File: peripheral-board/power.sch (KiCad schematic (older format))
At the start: 37 parts, among them CON4001 BARREL_JACK, Q4001 IRLML2244TRPbF, U4001 AP1509, U4002 LM27313, U4003 LT3652

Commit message: minor fixes
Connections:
- no-connect marks 0 -> 1
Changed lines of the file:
@@
-$EndComp
-$Comp
-L PWR_FLAG #FLG061
-U 1 1 58A910EB
-P 1850 1750
-F 0 "#FLG061" H -900 525 50  0001 C CNN
-F 1 "PWR_FLAG" H 1850 1924 50  0000 C CNN
-F 2 "" H -900 450 50  0001 C CNN
-F 3 "" H -900 450 50  0001 C CNN
-	1    1850 1750
-	0    1    1    0
 $EndComp
 $Comp
@@
 Text Label 6000 2400 0    60   ~ 0
 CHRG_SENSE
+Connection ~ 10350 1650
+NoConn ~ 1800 1650
+$Comp
+L PWR_FLAG #FLG061
+U 1 1 58A9FA40
+P 5350 1000
+F 0 "#FLG061" H -1000 225 50  0001 C CNN
+F 1 "PWR_FLAG" H 5350 1174 50  0000 C CNN
+F 2 "" H -1000 150 50  0001 C CNN
+F 3 "" H -1000 150 50  0001 C CNN
+	1    5350 1000
+	1    0    0    -1
+$EndComp
+$Comp
+L PWR_FLAG #FLG062
+U 1 1 58A9FB2F
+P 5250 1550
+F 0 "#FLG062" H -1100 775 50  0001 C CNN
+F 1 "PWR_FLAG" H 5250 1724 50  0000 C CNN
+F 2 "" H -1100 700 50  0001 C CNN
+F 3 "" H -1100 700 50  0001 C CNN
+	1    5250 1550
+	1    0    0    -1
+$EndComp
 $EndSCHEMATC

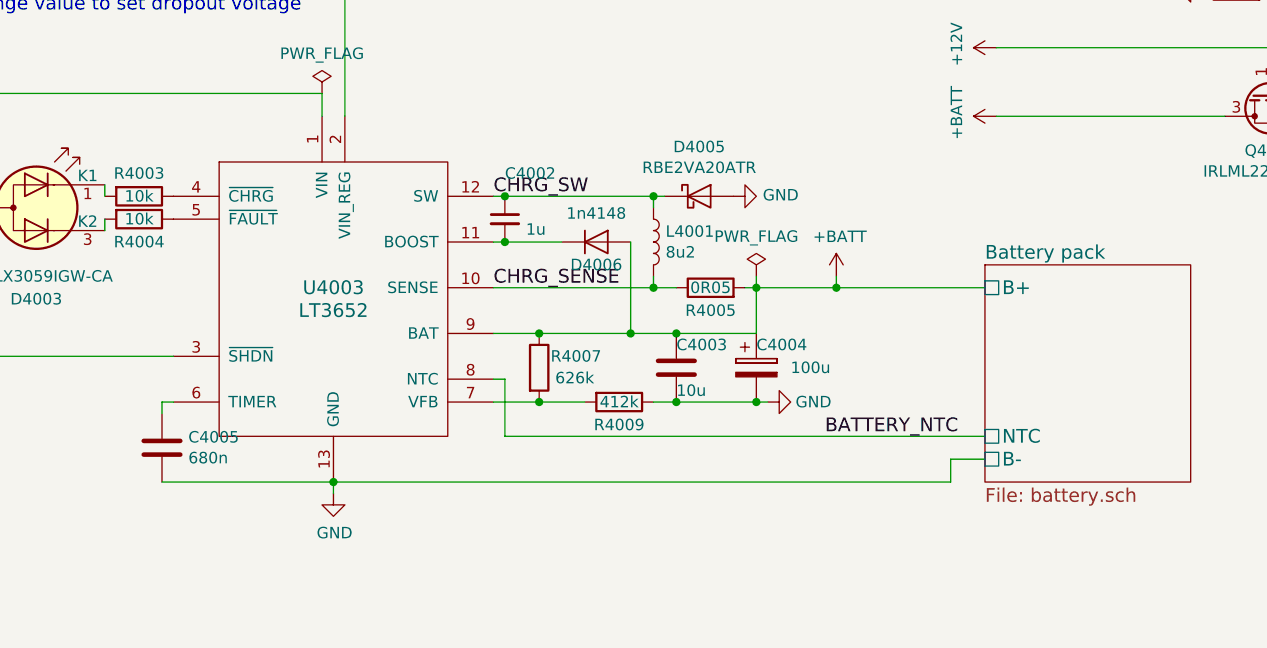
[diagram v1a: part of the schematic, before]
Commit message: added speaker and battery connectors
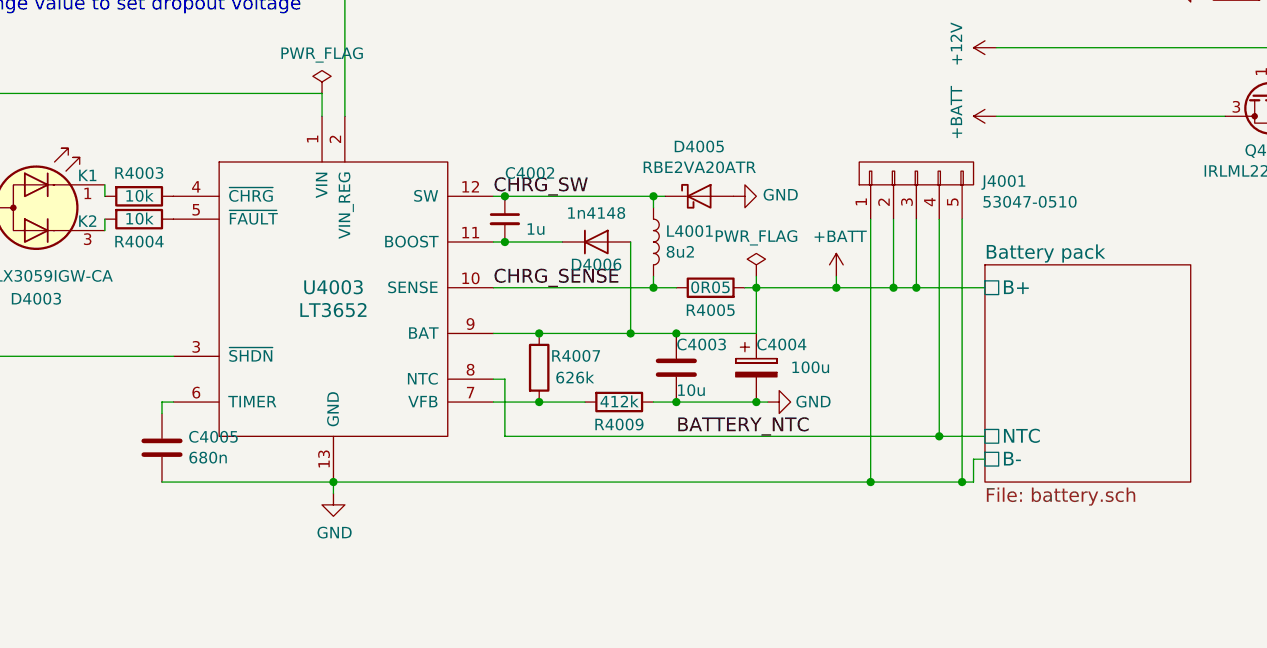
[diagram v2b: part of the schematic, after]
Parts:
- added J4001: 53047-0510, Connectors_Molex:Connector_Molex_PicoBlade_53047-0510, symbol CONN_01X05
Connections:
- net +BATT: now also J4001.2 (P2), J4001.3 (P3)
- net BATTERY_NTC: now also J4001.4 (P4)
- net GND: now also J4001.1 (P1), J4001.5 (P5)
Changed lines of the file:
@@
 Text Notes 2000 2750 0    60   ~ 0
 Add shutdown input\n
-Text Label 7450 3050 0    60   ~ 0
+Text Label 6800 3050 0    60   ~ 0
 BATTERY_NTC
 $Comp
@@
 	1    0    0    -1
 $EndComp
-Wire Wire Line
-	6700 2900 7200 2900
-Connection ~ 7150 2900
-Connection ~ 6800 2900
-Wire Wire Line
-	7150 2600 6000 2600
-Connection ~ 6800 2600
-Connection ~ 6200 2600
-Wire Wire Line
-	6000 2900 6400 2900
-Connection ~ 6200 2900
-Wire Wire Line
-	6000 2800 6050 2800
-Wire Wire Line
-	6000 2400 6800 2400
-Wire Wire Line
-	6700 2400 6700 2350
-Wire Wire Line
-	7150 2350 7150 2600
-Wire Wire Line
-	7100 2400 8150 2400
-Connection ~ 6700 2400
-Connection ~ 7150 2400
-Wire Wire Line
-	6700 2050 6700 2000
-Wire Wire Line
-	6000 2000 6750 2000
-Connection ~ 6700 2000
-Connection ~ 6050 2000
-Wire Wire Line
-	6000 2200 6300 2200
-Connection ~ 6050 2200
-Wire Wire Line
-	6600 2200 6600 2600
-Connection ~ 6600 2600
-Wire Wire Line
-	7500 2350 7500 2400
-Connection ~ 7500 2400
-Wire Wire Line
-	4600 2900 4550 2900
-Wire Wire Line
-	4550 2900 4550 2950
-Wire Wire Line
-	5250 1650 5250 1550
-Wire Wire Line
-	5250 1550 3700 1550
-Wire Wire Line
-	1800 1550 3400 1550
-Wire Wire Line
-	3300 1350 3300 1600
-Connection ~ 3300 1550
-Wire Wire Line
-	4600 2700 3050 2700
-Wire Wire Line
-	3050 2650 3050 2750
-Connection ~ 3050 2700
-Wire Wire Line
-	3050 1000 3050 2350
-Wire Wire Line
-	3050 1000 5350 1000
-Wire Wire Line
-	5350 1000 5350 1650
-Wire Wire Line
-	3300 1050 3300 1000
-Connection ~ 3300 1000
-Wire Wire Line
-	1800 1750 1850 1750
-Wire Wire Line
-	1850 1750 1850 1800
-Wire Wire Line
-	1850 1550 1850 1300
-Wire Wire Line
-	2150 1550 2150 1300
-Connection ~ 1850 1550
-Connection ~ 2150 1550
-Wire Wire Line
-	8150 3050 6050 3050
-Wire Wire Line
-	6050 3050 6050 2800
-Wire Wire Line
-	4550 3250 8000 3250
-Wire Wire Line
-	8000 3250 8000 3150
-Wire Wire Line
-	8000 3150 8150 3150
-Connection ~ 5300 3250
-Wire Wire Line
-	5300 3300 5300 3250
-Connection ~ 9800 1650
-Wire Wire Line
-	9200 1650 8200 1650
-Wire Wire Line
-	8200 1350 9800 1350
-Connection ~ 9400 1350
-Wire Wire Line
-	9400 1100 9400 1350
-Wire Wire Line
-	3000 5600 3000 5750
-Wire Wire Line
-	9600 1650 10600 1650
-Wire Wire Line
-	7850 4600 7900 4600
-Wire Wire Line
-	7900 4400 7900 4650
-Connection ~ 7900 4600
-Wire Wire Line
-	7750 5700 9800 5700
-Connection ~ 7850 5700
-Connection ~ 7950 5700
-Wire Wire Line
-	9300 5700 9300 5550
-Connection ~ 8050 5700
-Wire Wire Line
-	8600 5550 8600 5700
-Connection ~ 8600 5700
-Wire Wire Line
-	7750 5750 7750 5700
-Wire Wire Line
-	8500 5100 9300 5100
-Wire Wire Line
-	9300 5100 9300 5250
-Wire Wire Line
-	9100 5200 10000 5200
-Connection ~ 9300 5200
-Wire Wire Line
-	8800 5200 8500 5200
-Wire Wire Line
-	8600 5250 8600 5200
-Connection ~ 8600 5200
-Wire Wire Line
-	3700 5000 3800 5000
-Wire Wire Line
-	3750 5000 3750 4450
-Connection ~ 3750 5000
-Wire Wire Line
-	3000 4400 3000 4500
-Wire Wire Line
-	3700 5100 3800 5100
-Wire Wire Line
-	3750 5100 3750 5400
-Connection ~ 3750 5100
-Connection ~ 3000 5700
-Wire Wire Line
-	4100 5100 4800 5100
-Wire Wire Line
-	4150 5000 4150 5300
-Wire Wire Line
-	4150 5000 4100 5000
-Wire Wire Line
-	4400 5100 4400 5150
-Connection ~ 4150 5100
-Wire Wire Line
-	4400 5700 4400 5450
-Connection ~ 3750 5700
-Wire Wire Line
-	4150 5300 4100 5300
-Wire Wire Line
-	3750 5300 3800 5300
-Connection ~ 3750 5300
-Wire Wire Line
-	4800 5100 4800 5000
-Connection ~ 4400 5100
-Wire Wire Line
-	4500 5000 4500 5100
-Connection ~ 4500 5100
-Wire Wire Line
-	4400 5700 3000 5700
-Wire Wire Line
-	9800 5250 9800 5200
-Connection ~ 9800 5200
-Wire Wire Line
-	9800 5700 9800 5550
-Connection ~ 9300 5700
-Connection ~ 9900 5200
-Wire Wire Line
-	3700 1550 3700 2050
-Connection ~ 3700 1550
-Wire Wire Line
-	4300 2000 4300 1950
-Wire Wire Line
-	4300 2100 4300 2150
-Wire Wire Line
-	2950 4450 3450 4450
-Connection ~ 3000 4450
 Text Label 6000 2000 0    60   ~ 0
 CHRG_SW
 Text Label 6000 2400 0    60   ~ 0
 CHRG_SENSE
-Connection ~ 10350 1650
 NoConn ~ 1800 1650
 $Comp
@@
 	1    0    0    -1
 $EndComp
+$Comp
+L CONN_01X05 J4001
+U 1 1 58AB7B70
+P 7850 1900
+F 0 "J4001" V 7815 1612 50  0000 R CNN
+F 1 "53047-0510" V 7724 1612 50  0000 R CNN
+F 2 "Connectors_Molex:Connector_Molex_PicoBlade_53047-0510" H -2350 -250 50  0001 C CNN
+F 3 "" H -2350 -250 50  0001 C CNN
+	1    7850 1900
+	0    -1   -1   0
+$EndComp
+Wire Wire Line
+	6700 2900 7200 2900
+Connection ~ 7150 2900
+Connection ~ 6800 2900
+Wire Wire Line
+	7150 2600 6000 2600
+Connection ~ 6800 2600
+Connection ~ 6200 2600
+Wire Wire Line
+	6000 2900 6400 2900
+Connection ~ 6200 2900
+Wire Wire Line
+	6000 2800 6050 2800
+Wire Wire Line
+	6000 2400 6800 2400
+Wire Wire Line
+	6700 2400 6700 2350
+Wire Wire Line
+	7150 2350 7150 2600
+Wire Wire Line
+	7100 2400 8150 2400
+Connection ~ 6700 2400
+Connection ~ 7150 2400
+Wire Wire Line
+	6700 2050 6700 2000
+Wire Wire Line
+	6000 2000 6750 2000
+Connection ~ 6700 2000
+Connection ~ 6050 2000
+Wire Wire Line
+	6000 2200 6300 2200
+Connection ~ 6050 2200
+Wire Wire Line
+	6600 2200 6600 2600
+Connection ~ 6600 2600
+Wire Wire Line
+	7500 2350 7500 2400
+Connection ~ 7500 2400
+Wire Wire Line
+	4600 2900 4550 2900
+Wire Wire Line
+	4550 2900 4550 2950
+Wire Wire Line
+	5250 1650 5250 1550
+Wire Wire Line
+	5250 1550 3700 1550
+Wire Wire Line
+	1800 1550 3400 1550
+Wire Wire Line
+	3300 1350 3300 1600
+Connection ~ 3300 1550
+Wire Wire Line
+	4600 2700 3050 2700
+Wire Wire Line
+	3050 2650 3050 2750
+Connection ~ 3050 2700
+Wire Wire Line
+	3050 1000 3050 2350
+Wire Wire Line
+	3050 1000 5350 1000
+Wire Wire Line
+	5350 1000 5350 1650
+Wire Wire Line
+	3300 1050 3300 1000
+Connection ~ 3300 1000
+Wire Wire Line
+	1800 1750 1850 1750
+Wire Wire Line
+	1850 1750 1850 1800
+Wire Wire Line
+	1850 1550 1850 1300
+Wire Wire Line
+	2150 1550 2150 1300
+Connection ~ 1850 1550
+Connection ~ 2150 1550
+Wire Wire Line
+	8150 3050 6050 3050
+Wire Wire Line
+	6050 3050 6050 2800
+Wire Wire Line
+	4550 3250 8100 3250
+Connection ~ 5300 3250
+Wire Wire Line
+	5300 3300 5300 3250
+Connection ~ 9800 1650
+Wire Wire Line
+	9200 1650 8200 1650
+Wire Wire Line
+	8200 1350 9800 1350
+Connection ~ 9400 1350
+Wire Wire Line
+	9400 1100 9400 1350
+Wire Wire Line
+	3000 5600 3000 5750
+Wire Wire Line
+	9600 1650 10600 1650
+Wire Wire Line
+	7850 4600 7900 4600
+Wire Wire Line
+	7900 4400 7900 4650
+Connection ~ 7900 4600
+Wire Wire Line
+	7750 5700 9800 5700
+Connection ~ 7850 5700
+Connection ~ 7950 5700
+Wire Wire Line
+	9300 5700 9300 5550
+Connection ~ 8050 5700
+Wire Wire Line
+	8600 5550 8600 5700
+Connection ~ 8600 5700
+Wire Wire Line
+	7750 5750 7750 5700
+Wire Wire Line
+	8500 5100 9300 5100
+Wire Wire Line
+	9300 5100 9300 5250
+Wire Wire Line
+	9100 5200 10000 5200
+Connection ~ 9300 5200
+Wire Wire Line
+	8800 5200 8500 5200
+Wire Wire Line
+	8600 5250 8600 5200
+Connection ~ 8600 5200
+Wire Wire Line
+	3700 5000 3800 5000
+Wire Wire Line
+	3750 5000 3750 4450
+Connection ~ 3750 5000
+Wire Wire Line
+	3000 4400 3000 4500
+Wire Wire Line
+	3700 5100 3800 5100
+Wire Wire Line
+	3750 5100 3750 5400
+Connection ~ 3750 5100
+Connection ~ 3000 5700
+Wire Wire Line
+	4100 5100 4800 5100
+Wire Wire Line
+	4150 5000 4150 5300
+Wire Wire Line
+	4150 5000 4100 5000
+Wire Wire Line
+	4400 5100 4400 5150
+Connection ~ 4150 5100
+Wire Wire Line
+	4400 5700 4400 5450
+Connection ~ 3750 5700
+Wire Wire Line
+	4150 5300 4100 5300
+Wire Wire Line
+	3750 5300 3800 5300
+Connection ~ 3750 5300
+Wire Wire Line
+	4800 5100 4800 5000
+Connection ~ 4400 5100
+Wire Wire Line
+	4500 5000 4500 5100
+Connection ~ 4500 5100
+Wire Wire Line
+	4400 5700 3000 5700
+Wire Wire Line
+	9800 5250 9800 5200
+Connection ~ 9800 5200
+Wire Wire Line
+	9800 5700 9800 5550
+Connection ~ 9300 5700
+Connection ~ 9900 5200
+Wire Wire Line
+	3700 1550 3700 2050
+Connection ~ 3700 1550
+Wire Wire Line
+	4300 2000 4300 1950
+Wire Wire Line
+	4300 2100 4300 2150
+Wire Wire Line
+	2950 4450 3450 4450
+Connection ~ 3000 4450
+Connection ~ 10350 1650
+Wire Wire Line
+	7650 2100 7650 3250
+Connection ~ 7650 3250
+Wire Wire Line
+	7750 2100 7750 2400
+Connection ~ 7750 2400
+Wire Wire Line
+	7850 2100 7850 2400
+Connection ~ 7850 2400
+Wire Wire Line
+	7950 2100 7950 3050
+Connection ~ 7950 3050
+Wire Wire Line
+	8050 3250 8050 2100
+Wire Wire Line
+	8150 3150 8100 3150
+Wire Wire Line
+	8100 3150 8100 3250
+Connection ~ 8050 3250
 $EndSCHEMATC

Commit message: peripheral board all done o____O
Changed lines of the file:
@@
 $Descr A4 11693 8268
 encoding utf-8
-Sheet 4 10
+Sheet 4 8
 Title ""
 Date ""
@@
 	1    0    0    -1
 $EndComp
-$Sheet
-S 8150 2300 900  950
-U 589AAD6E
-F0 "Battery pack" 60
-F1 "battery.sch" 60
-F2 "B+" U L 8150 2400 60
-F3 "B-" U L 8150 3150 60
-F4 "NTC" U L 8150 3050 60
-$EndSheet
 $Comp
 L D_Schottky D4001
@@
 Wire Wire Line
 	7150 2350 7150 2600
-Wire Wire Line
-	7100 2400 8150 2400
 Connection ~ 6700 2400
 Connection ~ 7150 2400
@@
 	8100 3150 8100 3250
 Connection ~ 8050 3250
+Wire Wire Line
+	7100 2400 8150 2400
 $EndSCHEMATC

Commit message: minor fixes to peripheral board
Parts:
- L4002: value 10u -> 8u2
- R4012: value 270k -> 220k
- R4013: value 13.3k -> 12k
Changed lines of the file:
@@
 $EndComp
 $Comp
-L GND #PWR036
+L GND #PWR4008
 U 1 1 589A1FA0
 P 7050 2000
-F 0 "#PWR036" H -1000 100 50  0001 C CNN
+F 0 "#PWR4008" H -1000 100 50  0001 C CNN
 F 1 "GND" V 7055 1872 50  0000 R CNN
 F 2 "" H -1000 350 50  0001 C CNN
@@
 $EndComp
 $Comp
-L GND #PWR037
+L GND #PWR4010
 U 1 1 589A2378
 P 7200 2900
-F 0 "#PWR037" H 7250 2950 50  0001 C CNN
+F 0 "#PWR4010" H 7250 2950 50  0001 C CNN
 F 1 "GND" V 7200 2700 50  0000 C CNN
 F 2 "" H -750 100 50  0001 C CNN
@@
 $EndComp
 $Comp
-L +BATT #PWR038
+L +BATT #PWR4009
 U 1 1 589A3E06
 P 7500 2350
-F 0 "#PWR038" H -350 800 50  0001 C CNN
+F 0 "#PWR4009" H -350 800 50  0001 C CNN
 F 1 "+BATT" H 7515 2523 50  0000 C CNN
 F 2 "" H -350 950 50  0001 C CNN
@@
 $EndComp
 $Comp
-L GND #PWR039
+L GND #PWR4012
 U 1 1 589A4F62
 P 5300 3300
-F 0 "#PWR039" H -750 -100 50  0001 C CNN
+F 0 "#PWR4012" H -750 -100 50  0001 C CNN
 F 1 "GND" H 5305 3127 50  0000 C CNN
 F 2 "" H -750 150 50  0001 C CNN
@@
 $EndComp
 $Comp
-L GND #PWR040
+L GND #PWR4007
 U 1 1 589A711D
 P 3300 1900
-F 0 "#PWR040" H -250 -1350 50  0001 C CNN
+F 0 "#PWR4007" H -250 -1350 50  0001 C CNN
 F 1 "GND" H 3305 1727 50  0000 C CNN
 F 2 "" H -250 -1100 50  0001 C CNN
@@
 $EndComp
 $Comp
-L GND #PWR041
+L GND #PWR4011
 U 1 1 589A7BC3
 P 3050 3050
-F 0 "#PWR041" H -500 -200 50  0001 C CNN
+F 0 "#PWR4011" H -500 -200 50  0001 C CNN
 F 1 "GND" H 3055 2877 50  0000 C CNN
 F 2 "" H -500 50  50  0001 C CNN
@@
 $EndComp
 $Comp
-L GND #PWR042
+L GND #PWR4006
 U 1 1 589A855C
 P 1850 1800
-F 0 "#PWR042" H -850 -600 50  0001 C CNN
+F 0 "#PWR4006" H -850 -600 50  0001 C CNN
 F 1 "GND" H 1855 1627 50  0000 C CNN
 F 2 "" H -850 -350 50  0001 C CNN
@@
 $EndComp
 $Comp
-L +12V #PWR043
+L +12V #PWR4002
 U 1 1 589A8BB3
 P 2150 1300
-F 0 "#PWR043" H -950 100 50  0001 C CNN
+F 0 "#PWR4002" H -950 100 50  0001 C CNN
 F 1 "+12V" H 2165 1473 50  0000 C CNN
 F 2 "" H -950 250 50  0001 C CNN
@@
 $EndComp
 $Comp
-L PWR_FLAG #FLG044
+L PWR_FLAG #FLG4002
 U 1 1 589A8CB7
 P 1850 1300
-F 0 "#FLG044" H -900 75  50  0001 C CNN
+F 0 "#FLG4002" H -900 75  50  0001 C CNN
 F 1 "PWR_FLAG" H 1850 1474 50  0000 C CNN
 F 2 "" H -900 0   50  0001 C CNN
@@
 BATTERY_NTC
 $Comp
-L PWR_FLAG #FLG045
+L PWR_FLAG #FLG4005
 U 1 1 589AA4ED
 P 7150 2350
-F 0 "#FLG045" H 7200 2400 50  0001 C CNN
+F 0 "#FLG4005" H 7200 2400 50  0001 C CNN
 F 1 "PWR_FLAG" H 7150 2524 50  0000 C CNN
 F 2 "" H -900 -650 50  0001 C CNN
@@
 $EndComp
 $Comp
-L +BATT #PWR046
+L +BATT #PWR4004
 U 1 1 589B38CB
 P 8200 1650
-F 0 "#PWR046" H 350 100 50  0001 C CNN
+F 0 "#PWR4004" H 350 100 50  0001 C CNN
 F 1 "+BATT" H 8215 1823 50  0000 C CNN
 F 2 "" H 350 250 50  0001 C CNN
@@
 $EndComp
 $Comp
-L +12V #PWR047
+L +12V #PWR4003
 U 1 1 589B39F6
 P 8200 1350
-F 0 "#PWR047" H 5100 150 50  0001 C CNN
+F 0 "#PWR4003" H 5100 150 50  0001 C CNN
 F 1 "+12V" H 8215 1523 50  0000 C CNN
 F 2 "" H 5100 300 50  0001 C CNN
@@
 $EndComp
 $Comp
-L GND #PWR048
+L GND #PWR4001
 U 1 1 589B4E54
 P 9100 1100
-F 0 "#PWR048" H 5850 -2700 50  0001 C CNN
+F 0 "#PWR4001" H 5850 -2700 50  0001 C CNN
 F 1 "GND" V 9105 972 50  0000 R CNN
 F 2 "" H 5850 -2450 50  0001 C CNN
@@
 $EndComp
 $Comp
-L PWR_FLAG #FLG049
+L PWR_FLAG #FLG4004
 U 1 1 589B64BF
 P 10350 1650
-F 0 "#FLG049" H 6000 -2675 50  0001 C CNN
+F 0 "#FLG4004" H 6000 -2675 50  0001 C CNN
 F 1 "PWR_FLAG" H 10350 1824 50  0000 C CNN
 F 2 "" H 6000 -2750 50  0001 C CNN
@@
 $EndComp
 $Comp
-L GND #PWR050
+L GND #PWR4016
 U 1 1 589B8109
 P 7550 4600
-F 0 "#PWR050" H 7600 4650 50  0001 C CNN
+F 0 "#PWR4016" H 7600 4650 50  0001 C CNN
 F 1 "GND" V 7555 4472 50  0000 R CNN
 F 2 "" H 500 -200 50  0001 C CNN
@@
 $EndComp
 $Comp
-L GND #PWR051
+L GND #PWR4020
 U 1 1 589B85D2
 P 7750 5750
-F 0 "#PWR051" H 7800 5800 50  0001 C CNN
+F 0 "#PWR4020" H 7800 5800 50  0001 C CNN
 F 1 "GND" H 7755 5577 50  0000 C CNN
 F 2 "" H 650 -750 50  0001 C CNN
@@
 $EndComp
 $Comp
-L +3V3 #PWR052
+L +3V3 #PWR4018
 U 1 1 589B91D5
 P 9900 5200
-F 0 "#PWR052" H 9950 5250 50  0001 C CNN
+F 0 "#PWR4018" H 9950 5250 50  0001 C CNN
 F 1 "+3V3" H 9915 5373 50  0000 C CNN
 F 2 "" H 1700 -500 50  0001 C CNN
@@
 $EndComp
 $Comp
-L PWR_FLAG #FLG053
+L PWR_FLAG #FLG4007
 U 1 1 589B9237
 P 10000 5200
-F 0 "#FLG053" H 10050 5250 50  0001 C CNN
+F 0 "#FLG4007" H 10050 5250 50  0001 C CNN
 F 1 "PWR_FLAG" H 10000 5374 50  0000 C CNN
 F 2 "" H 1750 -550 50  0001 C CNN
@@
 P 3600 4450
 F 0 "L4002" V 3790 4450 50  0000 C CNN
-F 1 "10u" V 3699 4450 50  0000 C CNN
+F 1 "8u2" V 3699 4450 50  0000 C CNN
 F 2 "Choke_SMD:Choke_SMD_6.3x6.3_H3" H -1850 -550 50  0001 C CNN
 F 3 "" H -1850 -550 50  0001 C CNN
@@
 $EndComp
 $Comp
-L GND #PWR054
+L GND #PWR4015
 U 1 1 589BA9B7
 P 2650 4450
-F 0 "#PWR054" H 2700 4500 50  0001 C CNN
+F 0 "#PWR4015" H 2700 4500 50  0001 C CNN
 F 1 "GND" V 2655 4322 50  0000 R CNN
 F 2 "" H -4450 -2050 50  0001 C CNN
@@
 $EndComp
 $Comp
-L GND #PWR055
+L GND #PWR4019
 U 1 1 589BAA61
 P 3000 5750
-F 0 "#PWR055" H 3050 5800 50  0001 C CNN
+F 0 "#PWR4019" H 3050 5800 50  0001 C CNN
 F 1 "GND" H 3005 5577 50  0000 C CNN
 F 2 "" H -4100 -750 50  0001 C CNN
@@
 P 3950 5100
 F 0 "R4012" V 3850 5150 50  0000 C CNN
-F 1 "270k" V 3950 5100 50  0000 C CNN
+F 1 "220k" V 3950 5100 50  0000 C CNN
 F 2 "Resistors_SMD:R_0805" V -1070 -400 50  0001 C CNN
 F 3 "" H -1000 -400 50  0001 C CNN
@@
 P 3750 5550
 F 0 "R4013" H 3450 5550 50  0000 L CNN
-F 1 "13.3k" H 3500 5450 50  0000 L CNN
+F 1 "12k" H 3500 5450 50  0000 L CNN
 F 2 "Resistors_SMD:R_0805" V -1420 -200 50  0001 C CNN
 F 3 "" H -1350 -200 50  0001 C CNN
@@
 $EndComp
 $Comp
-L +24V #PWR056
+L +24V #PWR4017
 U 1 1 589BBC33
 P 4800 5000
-F 0 "#PWR056" H 4850 5050 50  0001 C CNN
+F 0 "#PWR4017" H 4850 5050 50  0001 C CNN
 F 1 "+24V" H 4815 5173 50  0000 C CNN
 F 2 "" H -100 -50 50  0001 C CNN
@@
 $EndComp
 $Comp
-L PWR_FLAG #FLG057
+L PWR_FLAG #FLG4006
 U 1 1 589BBD5B
 P 4500 5000
-F 0 "#FLG057" H 4550 5050 50  0001 C CNN
+F 0 "#FLG4006" H 4550 5050 50  0001 C CNN
 F 1 "PWR_FLAG" H 4500 5174 50  0000 C CNN
 F 2 "" H -400 -550 50  0001 C CNN
@@
 ~SHDN_24
 $Comp
-L VAA #PWR058
+L VAA #PWR4005
 U 1 1 58A8EB71
 P 10600 1650
-F 0 "#PWR058" H 10650 1700 50  0001 C CNN
+F 0 "#PWR4005" H 10650 1700 50  0001 C CNN
 F 1 "VAA" H 10617 1823 50  0000 C CNN
 F 2 "" H -250 900 50  0001 C CNN
@@
 $EndComp
 $Comp
-L VAA #PWR059
+L VAA #PWR4014
 U 1 1 58A8ECBE
 P 7900 4400
-F 0 "#PWR059" H 7950 4450 50  0001 C CNN
+F 0 "#PWR4014" H 7950 4450 50  0001 C CNN
 F 1 "VAA" H 7917 4573 50  0000 C CNN
 F 2 "" H -2950 3650 50  0001 C CNN
@@
 $EndComp
 $Comp
-L VAA #PWR060
+L VAA #PWR4013
 U 1 1 58A8F0E4
 P 3000 4400
-F 0 "#PWR060" H 3050 4450 50  0001 C CNN
+F 0 "#PWR4013" H 3050 4450 50  0001 C CNN
 F 1 "VAA" H 3017 4573 50  0000 C CNN
 F 2 "" H -7850 3650 50  0001 C CNN
@@
 NoConn ~ 1800 1650
 $Comp
-L PWR_FLAG #FLG061
+L PWR_FLAG #FLG4001
 U 1 1 58A9FA40
 P 5350 1000
-F 0 "#FLG061" H -1000 225 50  0001 C CNN
+F 0 "#FLG4001" H -1000 225 50  0001 C CNN
 F 1 "PWR_FLAG" H 5350 1174 50  0000 C CNN
 F 2 "" H -1000 150 50  0001 C CNN
@@
 $EndComp
 $Comp
-L PWR_FLAG #FLG062
+L PWR_FLAG #FLG4003
 U 1 1 58A9FB2F
 P 5250 1550
-F 0 "#FLG062" H -1100 775 50  0001 C CNN
+F 0 "#FLG4003" H -1100 775 50  0001 C CNN
 F 1 "PWR_FLAG" H 5250 1724 50  0000 C CNN
 F 2 "" H -1100 700 50  0001 C CNN
